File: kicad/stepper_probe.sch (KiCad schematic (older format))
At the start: 44 parts, among them J1 Conn_01x04_Male, J2 Conn_01x04_Male, J3 BAT, J4 Serial Port, J5 SWD, J6 BAT, M1 Motor, SW1 SW_Push, U1 TMCS1108A4BQDT, U2 TMCS1108A4BQDT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

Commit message: More PCB cleanup.
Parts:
- U1, U2: footprint stepper_probe:SOIC-8-N7_3.9x4.9mm_P1.27mm -> Package_SO:SOIC-8_3.9x4.9mm_P1.27mm
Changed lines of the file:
@@
 F 0 "U1" H 3925 1150 50  0000 C CNN
 F 1 "TMCS1108A4BQDT" H 4075 1250 50  0000 C CNN
-F 2 "stepper_probe:SOIC-8-N7_3.9x4.9mm_P1.27mm" H 4125 1650 50  0001 L CIN
+F 2 "Package_SO:SOIC-8_3.9x4.9mm_P1.27mm" H 4125 1650 50  0001 L CIN
 F 3 "" H 3725 1700 50  0001 C CNN
 	1    3725 1700
@@
 F 0 "U2" H 2950 2300 50  0000 C CNN
 F 1 "TMCS1108A4BQDT" H 3200 2375 50  0000 C CNN
-F 2 "stepper_probe:SOIC-8-N7_3.9x4.9mm_P1.27mm" H 3150 2725 50  0001 L CIN
+F 2 "Package_SO:SOIC-8_3.9x4.9mm_P1.27mm" H 3150 2725 50  0001 L CIN
 F 3 "" H 2750 2775 50  0001 C CNN
 	1    2750 2775
@@
 	7600 2100 8075 2100
 $Comp
-L stepper_probe:GND #PWR?
+L stepper_probe:GND #PWR0107
 U 1 1 62F7645D
 P 7900 1350
-F 0 "#PWR?" H 7900 1100 50  0001 C CNN
+F 0 "#PWR0107" H 7900 1100 50  0001 C CNN
 F 1 "GND" H 7904 1195 50  0001 C CNN
 F 2 "" H 7900 1350 50  0001 C CNN

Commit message: Production files with JLCPCB order.
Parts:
- C1: LCSC (none) -> C52923; LCSC Part Number C52923 -> (none)
- C10, C11, C2: LCSC (none) -> C96446; LCSC Part Number C96446 -> (none)
- C12, C4, C6, C8, C9: LCSC (none) -> C307331; LCSC Part Number C307331 -> (none)
- C3, C5: LCSC (none) -> C26406; LCSC Part Number C26406 -> (none)
- C7: LCSC (none) -> C440198; LCSC Part Number C440198 -> (none)
- D1: value LED -> LED R; LCSC (none) -> C165980; LCSC Part Number C165980 -> (none)
- D2: value LED -> LED Y; LCSC (none) -> C165978; LCSC Part Number C165980 -> (none)
- D3: value LED -> LED R; LCSC (none) -> C165980; LCSC Part Number C165978 -> (none)
- D4, D5: LCSC (none) -> C232821; LCSC Part Number C232821 -> (none)
- D6: LCSC (none) -> C191023; LCSC Part Number C191023 -> (none)
- J5: LCSC (none) -> C2935458; LCSC Part Number C2935458 -> (none)
- L2: LCSC (none) -> C107342; LCSC Part Number C107342 -> (none)
- L3: LCSC (none) -> C27143; LCSC Part Number C27143 -> (none)
- R1, R2, R3, R4: LCSC (none) -> C25077; LCSC Part Number C25077 -> (none)
- R10: LCSC (none) -> C25744; LCSC Part Number C25744 -> (none)
- R5, R6, R7: LCSC (none) -> C25905; LCSC Part Number C25905 -> (none)
- R8, R9: LCSC (none) -> C11702; LCSC Part Number C11702 -> (none)
- SW1: LCSC (none) -> C720477; LCSC Part Number C720477 -> (none)
- U4: LCSC (none) -> C2692194
- U5: LCSC (none) -> C7562; LCSC Part Number C7562 -> (none)
- Y1: LCSC (none) -> C479190; LCSC Part Number C479190 -> (none)

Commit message: Added calibration battery pads.
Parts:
- added C13, C14: DNI, stepper_probe:C_0402_1005Metric_Pad0.74x0.62mm_HandSolder, symbol Device:C
- added J7: Conn_01x01_Female, stepper_probe:BAT_PLUS_PAD, symbol Connector:Conn_01x01_Female
- added J8: Conn_01x01_Female, stepper_probe:BAT_MINUS_PAD, symbol Connector:Conn_01x01_Female
- M1: symbol simple_stepper_motor_analyzer:Motor -> stepper_probe-rescue:Motor-simple_stepper_motor_analyzer
- U1, U2: symbol simple_stepper_motor_analyzer:ACS70331_soic8 -> stepper_probe-rescue:ACS70331_soic8-simple_stepper_motor_analyzer
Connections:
- net labels added: BAT+
- wire segments 194 -> 203
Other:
- note added: "BLE STEPPER MOTOR MONITOR v1.3"
- note added: "OPTIONAL BAT"
- note added: "To zero calibrate the probe, disconnect all\ncables, touch the pads at the back of the\nboard with a +9V battery and press the\nbutton for 10 secs."
- note added: "Zero calibration\nbattery pads."
- note removed: "BAT"
- note removed: "BLE STEPPER MOTOR MONITOR v1.1"
- note removed: "Notes:\n* P26 was LED1\n* P25 was LED2\n* P09 was SENSOR_DIS"
- moved on the sheet: C12, D1, D2, D3, D6, J3, J4, J5, R10, R5, R6, R7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

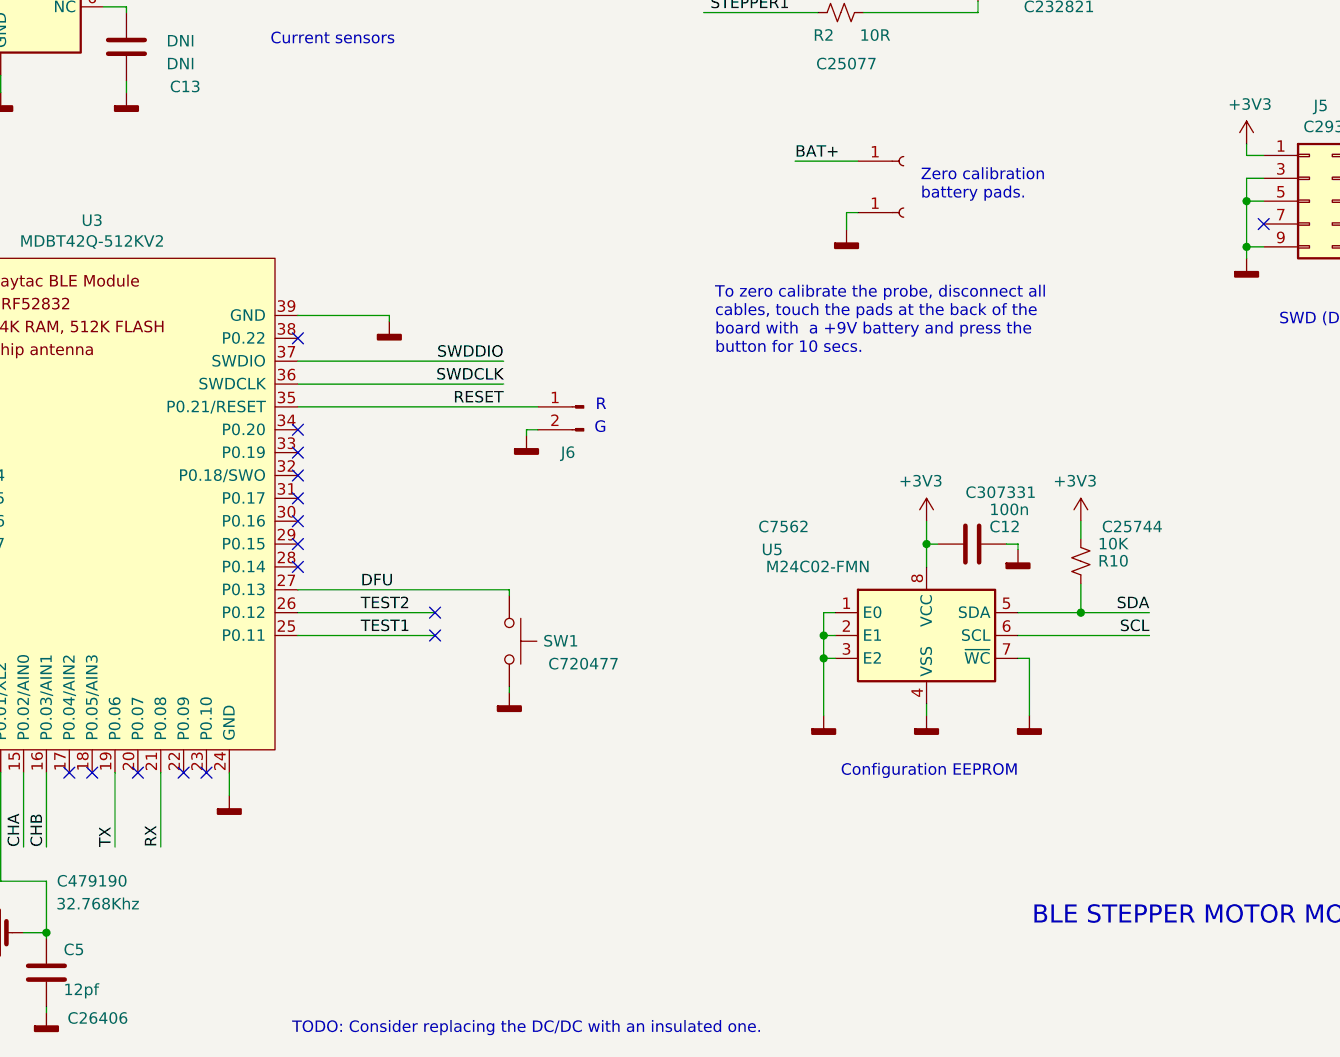
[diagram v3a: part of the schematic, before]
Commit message: Added configuration resistors.
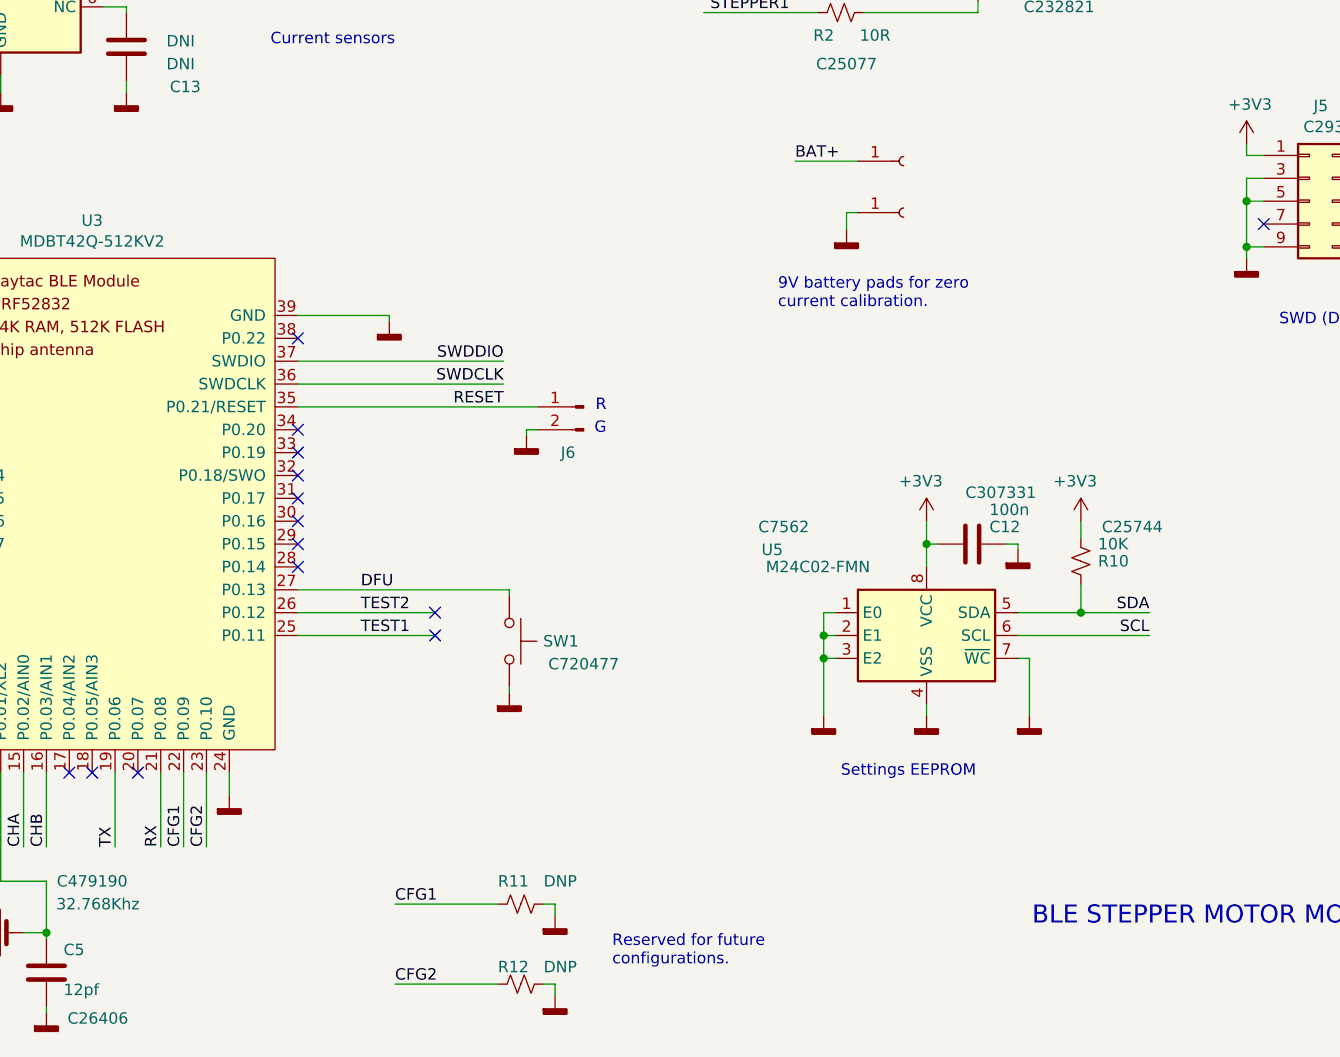
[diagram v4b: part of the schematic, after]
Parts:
- added R11, R12: DNP, stepper_probe:R_0402_1005Metric_Pad0.72x0.64mm_HandSolder, symbol Device:R_Small_US
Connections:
- net labels added: CFG1, CFG2
- wire segments 203 -> 211
- no-connect marks 22 -> 20
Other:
- note added: "9V battery pads for zero \ncurrent calibration."
- note added: "Reserved for future\nconfigurations."
- note added: "Settings EEPROM"
- note removed: "Configuration EEPROM"
- note removed: "TODO: Consider replacing the DC/DC with an insulated one."
- note removed: "To zero calibrate the probe, disconnect all\ncables, touch the pads at the back of the\nboard with a +9V battery and press the\nbutton for 10 secs."
- note removed: "Zero calibration\nbattery pads."
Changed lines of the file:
@@
 NoConn ~ 3100 6225
 NoConn ~ 3300 6225
-NoConn ~ 3600 6225
 NoConn ~ 4000 4925
 NoConn ~ 4000 5125
@@
 Wire Wire Line
 	3400 6225 3400 6550
-Text Notes 3975 7375 0    50   ~ 0
-TODO: Consider replacing the DC/DC with an insulated one.
 $Comp
 L stepper_probe:GND #PWR011
@@
 Text Label 1575 4825 0    50   ~ 0
 SCL
-NoConn ~ 3500 6225
 $Comp
 L stepper_probe:+3V3 #PWR0103
@@
 	7200 2100 7600 2100
 Text Notes 6375 6250 0    50   ~ 0
-Configuration EEPROM
+Settings EEPROM
 $Comp
 L stepper_probe:+3V3 #PWR0105
@@
 Text Label 6175 3550 0    50   ~ 0
 BAT+
-Text Notes 5825 4400 0    50   ~ 0
-To zero calibrate the probe, disconnect all\ncables, touch the pads at the back of the\nboard with  a +9V battery and press the\nbutton for 10 secs.
-Text Notes 6725 3725 0    50   ~ 0
-Zero calibration\nbattery pads.
 Wire Wire Line
 	7725 1025 8025 1025
+$Comp
+L stepper_probe:GND #PWR0111
+U 1 1 62EFA692
+P 5125 7200
+F 0 "#PWR0111" H 5125 6950 50  0001 C CNN
+F 1 "GND" H 5129 7045 50  0001 C CNN
+F 2 "" H 5125 7200 50  0001 C CNN
+F 3 "" H 5125 7200 50  0001 C CNN
+	1    5125 7200
+	1    0    0    -1
+$EndComp
+$Comp
+L stepper_probe:GND #PWR0112
+U 1 1 62EFAB50
+P 5125 6850
+F 0 "#PWR0112" H 5125 6600 50  0001 C CNN
+F 1 "GND" H 5129 6695 50  0001 C CNN
+F 2 "" H 5125 6850 50  0001 C CNN
+F 3 "" H 5125 6850 50  0001 C CNN
+	1    5125 6850
+	1    0    0    -1
+$EndComp
+$Comp
+L Device:R_Small_US R11
+U 1 1 62EFB038
+P 4975 6800
+F 0 "R11" V 5075 6900 50  0000 R CNN
+F 1 "DNP" V 5075 6700 50  0000 R CNN
+F 2 "stepper_probe:R_0402_1005Metric_Pad0.72x0.64mm_HandSolder" H 4975 6800 50  0001 C CNN
+F 3 "~" H 4975 6800 50  0001 C CNN
+	1    4975 6800
+	0    -1   -1   0
+$EndComp
+$Comp
+L Device:R_Small_US R12
+U 1 1 62EFBB37
+P 4975 7150
+F 0 "R12" V 5050 7250 50  0000 R CNN
+F 1 "DNP" V 5050 7050 50  0000 R CNN
+F 2 "stepper_probe:R_0402_1005Metric_Pad0.72x0.64mm_HandSolder" H 4975 7150 50  0001 C CNN
+F 3 "~" H 4975 7150 50  0001 C CNN
+	1    4975 7150
+	0    -1   -1   0
+$EndComp
+Wire Wire Line
+	5075 6800 5125 6800
+Wire Wire Line
+	5125 6800 5125 6850
+Wire Wire Line
+	5075 7150 5125 7150
+Wire Wire Line
+	5125 7150 5125 7200
+Text Label 4425 6800 0    50   ~ 0
+CFG1
+Wire Wire Line
+	4425 6800 4875 6800
+Wire Wire Line
+	4425 7150 4875 7150
+Text Label 4425 7150 0    50   ~ 0
+CFG2
+Wire Wire Line
+	3500 6225 3500 6550
+Wire Wire Line
+	3600 6225 3600 6550
+Text Label 3500 6550 1    50   ~ 0
+CFG1
+Text Label 3600 6550 1    50   ~ 0
+CFG2
+Text Notes 5375 7075 0    50   ~ 0
+Reserved for future\nconfigurations.
+Text Notes 6100 4200 0    50   ~ 0
+9V battery pads for zero \ncurrent calibration.
 $EndSCHEMATC

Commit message: .
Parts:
- C13, C14: LCSC DNI -> DNP
- J7, J8, M1, R11, R12: LCSC (none) -> DNP
- U1, U2: value TMCS1108A4BQDT -> CC6920BSO-5A; LCSC (none) -> C2880430
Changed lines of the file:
@@
 F 2 "stepper_probe:connector_4pins_horizontal" H 950 1650 50  0001 C CNN
 F 3 "~" H 950 1650 50  0001 C CNN
+F 4 "" H 950 1650 50  0001 C CNN "LCSC"
 	1    950  1650
 	1    0    0    1
@@
 F 3 "~" H 1275 2925 50  0001 C CNN
 F 4 "C31753" H 1350 3200 50  0000 C CNN "LCSC Part Number"
+F 5 "" H 1275 2925 50  0001 C CNN "LCSC"
 	1    1275 2925
 	1    0    0    1
@@
 P 3725 1700
 F 0 "U1" H 2850 1975 50  0000 C CNN
-F 1 "TMCS1108A4BQDT" H 3150 2125 50  0000 C CNN
+F 1 "CC6920BSO-5A" H 3150 2125 50  0000 C CNN
 F 2 "Package_SO:SOIC-8_3.9x4.9mm_P1.27mm" H 4125 1650 50  0001 L CIN
 F 3 "" H 3725 1700 50  0001 C CNN
+F 4 "C2880430" H 3725 1700 50  0000 C CNN "LCSC"
 	1    3725 1700
 	1    0    0    -1
@@
 F 2 "stepper_probe:Empty" H 1010 3115 50  0001 C CNN
 F 3 "" H 1010 3115 50  0001 C CNN
+F 4 "DNP" H 1000 3025 50  0001 C CNN "LCSC"
 	1    1000 3025
 	0    -1   -1   0
@@
 	1    0    0    -1
 $EndComp
-Text Notes 4425 3050 2    50   ~ 0
-Current sensors
 $Comp
 L Connector:Conn_01x02_Male J3
@@
 F 2 "stepper_probe:PinHeader_1x02_P2.54mm_Vertical" H 8225 1025 50  0001 C CNN
 F 3 "~" H 8225 1025 50  0001 C CNN
+F 4 "" H 8225 1025 50  0001 C CNN "LCSC"
 	1    8225 1025
 	-1   0    0    -1
@@
 F 2 "stepper_probe:C_0402_1005Metric_Pad0.74x0.62mm_HandSolder" H 3938 1075 50  0001 C CNN
 F 3 "~" H 3900 1225 50  0001 C CNN
-F 4 "C307331" V 3750 1325 50  0000 C CNN "LCSC"
+F 4 "C307331" V 3850 350 50  0000 C CNN "LCSC"
 	1    3900 1225
 	0    1    1    0
@@
 F 2 "stepper_probe:PinHeader_1x04_P2.54mm_Vertical" H 10375 3675 50  0001 C CNN
 F 3 "~" H 10375 3675 50  0001 C CNN
+F 4 "" H 10375 3675 50  0001 C CNN "LCSC"
 	1    10375 3675
 	-1   0    0    -1
@@
 F 2 "stepper_probe:PinHeader_1x02_P2.54mm_Vertical" H 5250 4625 50  0001 C CNN
 F 3 "~" H 5250 4625 50  0001 C CNN
+F 4 "" H 5250 4625 50  0001 C CNN "LCSC"
 	1    5250 4625
 	-1   0    0    -1
@@
 F 2 "stepper_probe:C_0402_1005Metric_Pad0.74x0.62mm_HandSolder" H 3288 2900 50  0001 C CNN
 F 3 "~" H 3250 3050 50  0001 C CNN
-F 4 "DNI" H 3075 3125 50  0000 R CNN "LCSC"
+F 4 "DNP" H 3075 3125 50  0000 R CNN "LCSC"
 	1    3250 3050
 	-1   0    0    1
@@
 U 1 1 627AA0D1
 P 2750 2775
-F 0 "U2" H 1975 2225 50  0000 C CNN
-F 1 "TMCS1108A4BQDT" H 2250 2350 50  0000 C CNN
+F 0 "U2" H 2000 2450 50  0000 C CNN
+F 1 "CC6920BSO-5A" H 2250 2350 50  0000 C CNN
 F 2 "Package_SO:SOIC-8_3.9x4.9mm_P1.27mm" H 3150 2725 50  0001 L CIN
 F 3 "" H 2750 2775 50  0001 C CNN
+F 4 "C2880430" H 2150 2250 50  0000 C CNN "LCSC"
 	1    2750 2775
 	1    0    0    -1
@@
 F 2 "stepper_probe:C_0402_1005Metric_Pad0.74x0.62mm_HandSolder" H 4263 1825 50  0001 C CNN
 F 3 "~" H 4225 1975 50  0001 C CNN
-F 4 "DNI" H 4050 2050 50  0000 R CNN "LCSC"
+F 4 "DNP" H 4050 2050 50  0000 R CNN "LCSC"
 	1    4225 1975
 	-1   0    0    1
@@
 F 2 "stepper_probe:BAT_PLUS_PAD" H 6650 3550 50  0001 C CNN
 F 3 "~" H 6650 3550 50  0001 C CNN
+F 4 "DNP" H 6650 3550 50  0001 C CNN "LCSC"
 	1    6650 3550
 	1    0    0    -1
@@
 F 2 "stepper_probe:BAT_MINUS_PAD" H 6650 3775 50  0001 C CNN
 F 3 "~" H 6650 3775 50  0001 C CNN
+F 4 "DNP" H 6650 3775 50  0001 C CNN "LCSC"
 	1    6650 3775
 	1    0    0    -1
@@
 F 2 "stepper_probe:R_0402_1005Metric_Pad0.72x0.64mm_HandSolder" H 4975 6800 50  0001 C CNN
 F 3 "~" H 4975 6800 50  0001 C CNN
+F 4 "DNP" H 4975 6800 50  0001 C CNN "LCSC"
 	1    4975 6800
 	0    -1   -1   0
@@
 F 2 "stepper_probe:R_0402_1005Metric_Pad0.72x0.64mm_HandSolder" H 4975 7150 50  0001 C CNN
 F 3 "~" H 4975 7150 50  0001 C CNN
+F 4 "DNP" H 4975 7150 50  0001 C CNN "LCSC"
 	1    4975 7150
 	0    -1   -1   0
@@
 Text Notes 6100 4200 0    50   ~ 0
 9V battery pads for zero \ncurrent calibration.
+Text Notes 3925 3025 0    50   ~ 0
+Current sensors
 $EndSCHEMATC

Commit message: Moved SOIC footprint to local library. Before rotating for JLCPCB.
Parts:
- U1, U2, U5: footprint Package_SO:SOIC-8_3.9x4.9mm_P1.27mm -> stepper_probe:SOIC-8_LCPCB_ROT
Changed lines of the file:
@@
 F 0 "U1" H 2850 1975 50  0000 C CNN
 F 1 "CC6920BSO-5A" H 3150 2125 50  0000 C CNN
-F 2 "Package_SO:SOIC-8_3.9x4.9mm_P1.27mm" H 4125 1650 50  0001 L CIN
+F 2 "stepper_probe:SOIC-8_LCPCB_ROT" H 4125 1650 50  0001 L CIN
 F 3 "" H 3725 1700 50  0001 C CNN
 F 4 "C2880430" H 3725 1700 50  0000 C CNN "LCSC"
@@
 F 0 "U5" H 6075 6000 50  0000 C CNN
 F 1 "M24C02-FMN" H 6275 5925 50  0000 C CNN
-F 2 "Package_SO:SOIC-8_3.9x4.9mm_P1.27mm" H 6750 5975 50  0001 C CNN
+F 2 "stepper_probe:SOIC-8_LCPCB_ROT" H 6750 5975 50  0001 C CNN
 F 3 "http://www.st.com/content/ccc/resource/technical/document/datasheet/b0/d8/50/40/5a/85/49/6f/DM00071904.pdf/files/DM00071904.pdf/jcr:content/translations/en.DM00071904.pdf" H 6800 5125 50  0001 C CNN
 F 4 "C7562" H 6125 6100 50  0000 C CNN "LCSC"
@@
 F 0 "U2" H 2000 2450 50  0000 C CNN
 F 1 "CC6920BSO-5A" H 2250 2350 50  0000 C CNN
-F 2 "Package_SO:SOIC-8_3.9x4.9mm_P1.27mm" H 3150 2725 50  0001 L CIN
+F 2 "stepper_probe:SOIC-8_LCPCB_ROT" H 3150 2725 50  0001 L CIN
 F 3 "" H 2750 2775 50  0001 C CNN
 F 4 "C2880430" H 2150 2250 50  0000 C CNN "LCSC"

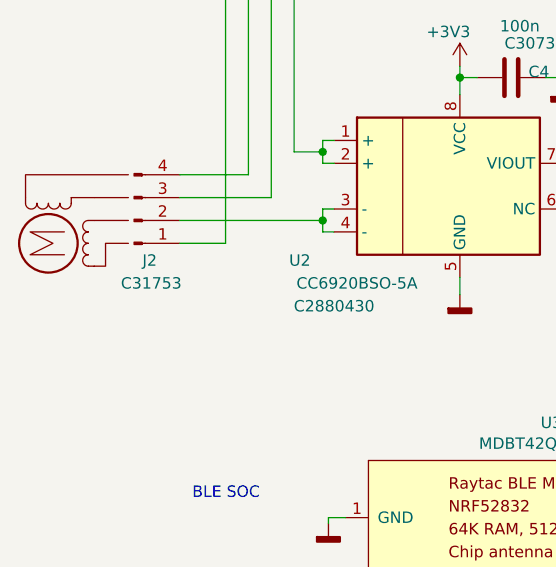
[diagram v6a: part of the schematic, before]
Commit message: Rotated footprints for JLCPCB orientation.
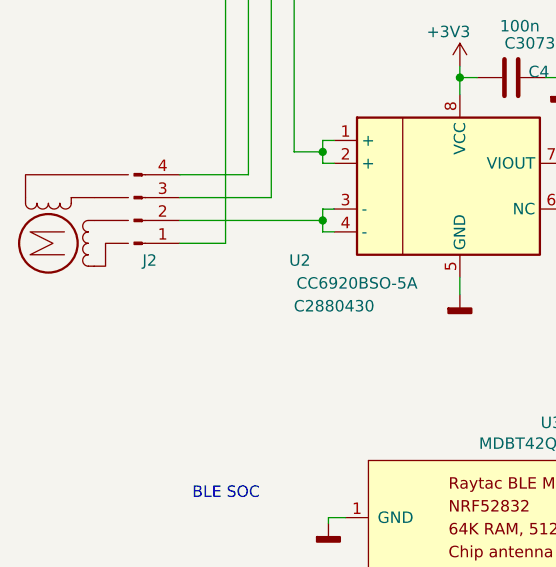
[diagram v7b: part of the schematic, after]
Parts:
- J1: LCSC (none) -> C31753
- J2: LCSC (none) -> C31753; LCSC Part Number C31753 -> (none)
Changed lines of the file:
@@
 F 2 "stepper_probe:connector_4pins_horizontal" H 950 1650 50  0001 C CNN
 F 3 "~" H 950 1650 50  0001 C CNN
-F 4 "" H 950 1650 50  0001 C CNN "LCSC"
+F 4 "C31753" H 950 1650 50  0001 C CNN "LCSC"
 	1    950  1650
 	1    0    0    1
@@
 F 2 "stepper_probe:connector_4pins_horizontal" H 1275 2925 50  0001 C CNN
 F 3 "~" H 1275 2925 50  0001 C CNN
-F 4 "C31753" H 1350 3200 50  0000 C CNN "LCSC Part Number"
-F 5 "" H 1275 2925 50  0001 C CNN "LCSC"
+F 4 "C31753" H 1275 2925 50  0001 C CNN "LCSC"
 	1    1275 2925
 	1    0    0    1

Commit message: Assorted tweaks.
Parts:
- added R13, R14, R15: 0R, stepper_probe:R_0402_1005Metric_Pad0.72x0.64mm_HandSolder, symbol Device:R_Small_US
- added R16, R17: 1K, stepper_probe:R_0402_1005Metric_Pad0.72x0.64mm_HandSolder, symbol Device:R_Small_US
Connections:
- net +3V3: now also R14.1, R15.2; no longer C10.1, C11.1, C2.1, C9.1, U3.11 (VDD), U4.3 (OUT)
- net BAT+: now also J3.2 (Pin_2); no longer J3.1 (Pin_1)
- net CHA: now also R16.1; no longer U1.7 (VIOUT)
- net CHB: now also R17.1; no longer U2.7 (VIOUT)
- net GND: now also J3.1 (Pin_1); no longer J3.2 (Pin_2)
- net at C7.1, C8.1, D4.1 (+)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: now also R13.2; no longer U4.1 (IN)
- new net: C10.1, C11.1, C9.1, R14.2, U4.3 (OUT)
- new net: R16.2, U1.7 (VIOUT)
- new net: R17.2, U2.7 (VIOUT)
- new net: C2.1, R15.1, U3.11 (VDD)
- new net: R13.1, U4.1 (IN)
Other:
- moved on the sheet: C10, C8, C9, U4
